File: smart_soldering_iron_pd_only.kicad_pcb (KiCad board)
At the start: 2 copper layers, 15 x 107.9 mm, 93 parts, among them J1 Conn_01x04_Pin, J2 TIP_SMALL_END, J3 TIP_MID, U3 ATMEGA328P-AU, U5 CH224K, X1 16MHz

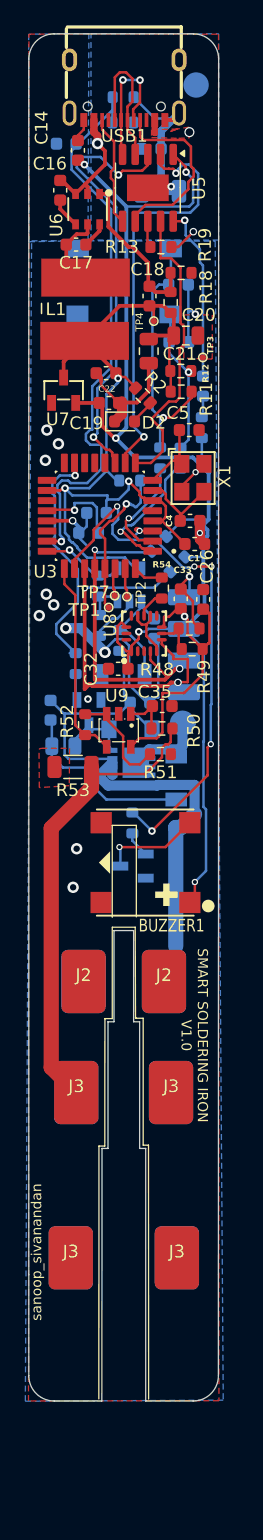
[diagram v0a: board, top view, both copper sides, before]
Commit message: added rgb led
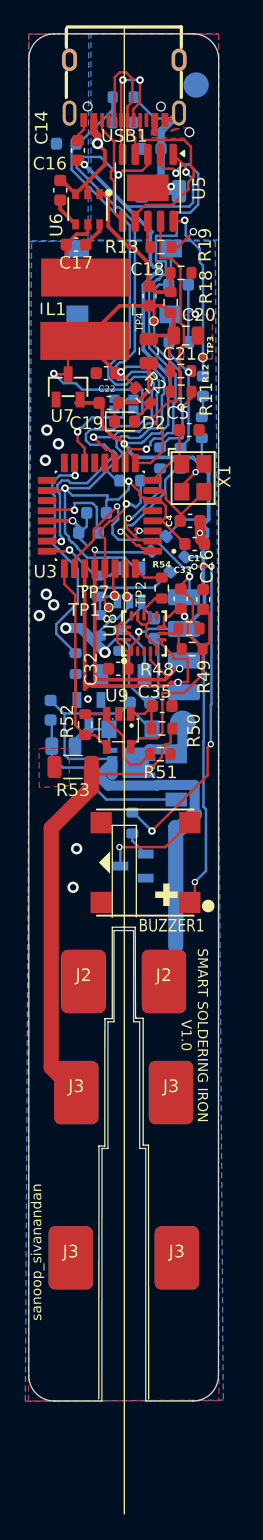
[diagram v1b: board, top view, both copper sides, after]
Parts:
- added LED1: ~, smart_soldering_iron:LED-SMD_4P-L1.6-W1.5_XL-1615RGBC-WS2812B-S, B.Cu at (229.0, 82.0)
- moved U7 0.44 mm to (224.6, 80.7)
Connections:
- U3 pad 14: unconnected-(U3-PB2-Pad14) -> LED_RGB
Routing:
- net VCC_5V: track 68.9 -> 87.2 mm, vias 3 -> 4
- net V_SENSE: track 45.0 -> 55.2 mm
- net CFG3: track 34.3 -> 43.4 mm
- net LED_RGB: track 0.00 -> 8.84 mm, vias 0 -> 1
- net VCC_3V3: track 125.9 -> 131.7 mm
- net GND: track 81.8 -> 78.9 mm
- net CFG2: track 33.6 -> 36.3 mm

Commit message: connected 5v to the tip amp measure
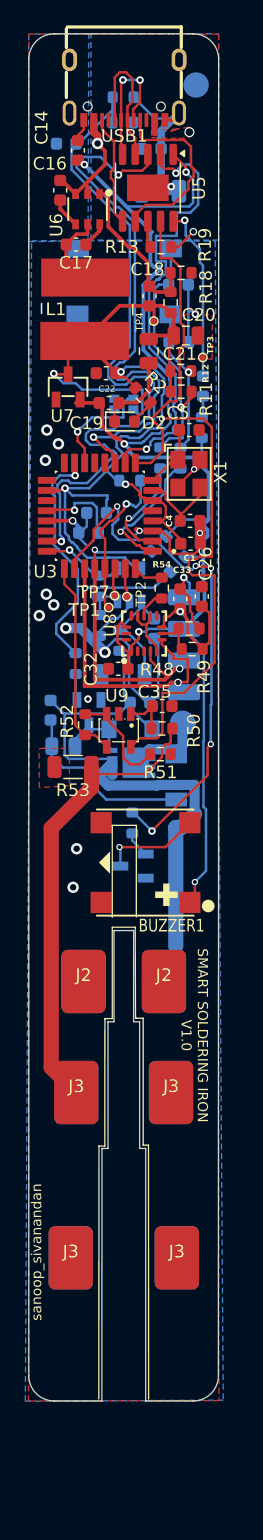
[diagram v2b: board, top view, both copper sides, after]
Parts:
- moved X1 0.45 mm to (234.2, 87.5)
- moved C1 0.33 mm to (234.3, 93.1)
- moved C26 0.25 mm to (235.2, 97.2)
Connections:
- U9 pad 5: VCC_3V3 -> VCC_5V
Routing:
- net VCC_5V: track 87.2 -> 122.1 mm, vias 4 -> 5
- net VCC_3V3: track 131.7 -> 120.7 mm
- net GND: track 78.9 -> 83.8 mm
